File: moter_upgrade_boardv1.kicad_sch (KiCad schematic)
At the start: 52 parts, among them J1 Conn_01x04_Socket, J2 Conn_01x03_Socket, J3 Conn_01x02_Socket, J4 Conn_01x03_Socket, J5 Conn_01x05_Socket, J6 USB_C_Receptacle_USB2.0_16P, J7 Conn_01x03_Socket, SW1 SW_SPDT, SW2 SW_Push, SW3 SW_Wuerth_450301014042, U1 BD33FC0FP, U2 TLP785, U3 TLP785, U4 STM32H523CCTx, U5 MCP2562-E-P, U6 CH340E, U7 BD33FC0FP

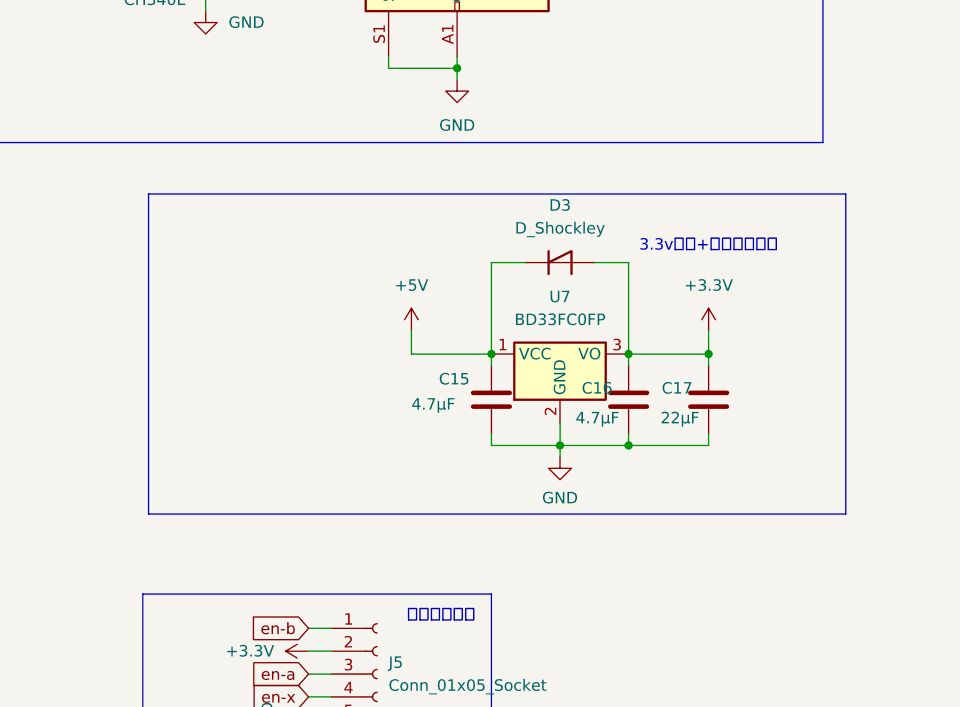
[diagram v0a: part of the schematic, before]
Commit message: 回路図の書き換え　部品配置配線のリセット
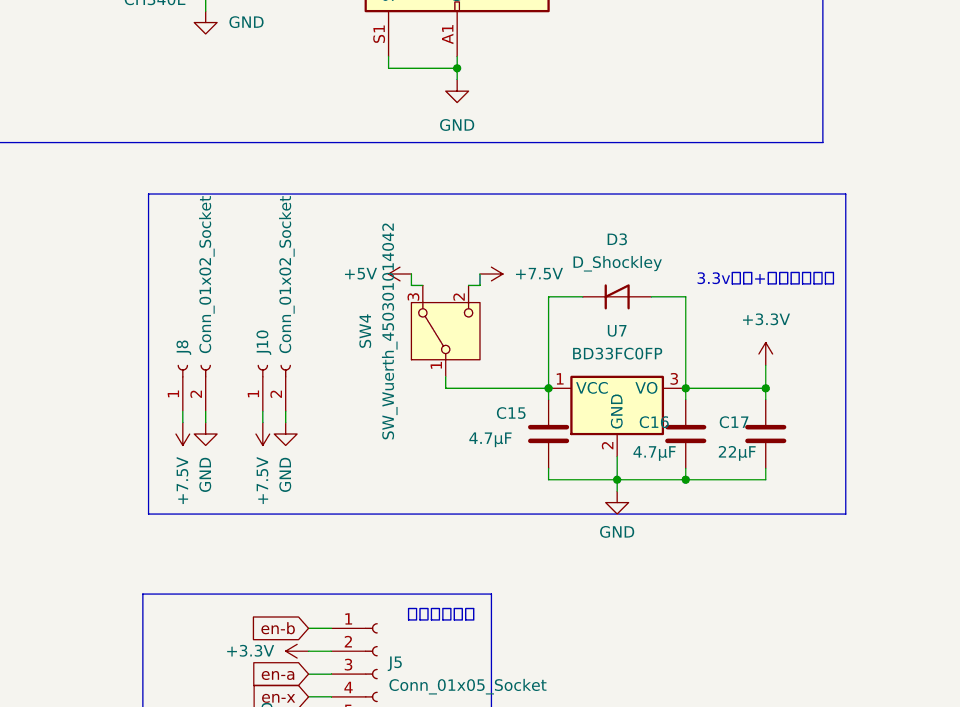
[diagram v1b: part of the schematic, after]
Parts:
- added J10, J8: Conn_01x02_Socket, symbol Connector:Conn_01x02_Socket
- added SW4: SW_Wuerth_450301014042, Button_Switch_THT:SW_Slide-03_Wuerth-WS-SLTV_10x2.5x6.4_P2.54mm, symbol Switch:SW_Wuerth_450301014042
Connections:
- net +5V: now also SW4.3 (A); no longer C15.1, D3.1 (K), U7.1 (VCC)
- net GND: now also J10.2 (Pin_2), J8.2 (Pin_2)
- new net: C15.1, D3.1 (K), SW4.1 (B), U7.1 (VCC)
- new net +7.5V: J10.1 (Pin_1), J8.1 (Pin_1), SW4.2 (C)
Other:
- moved on the sheet: C15, C16, C17, D3, U7

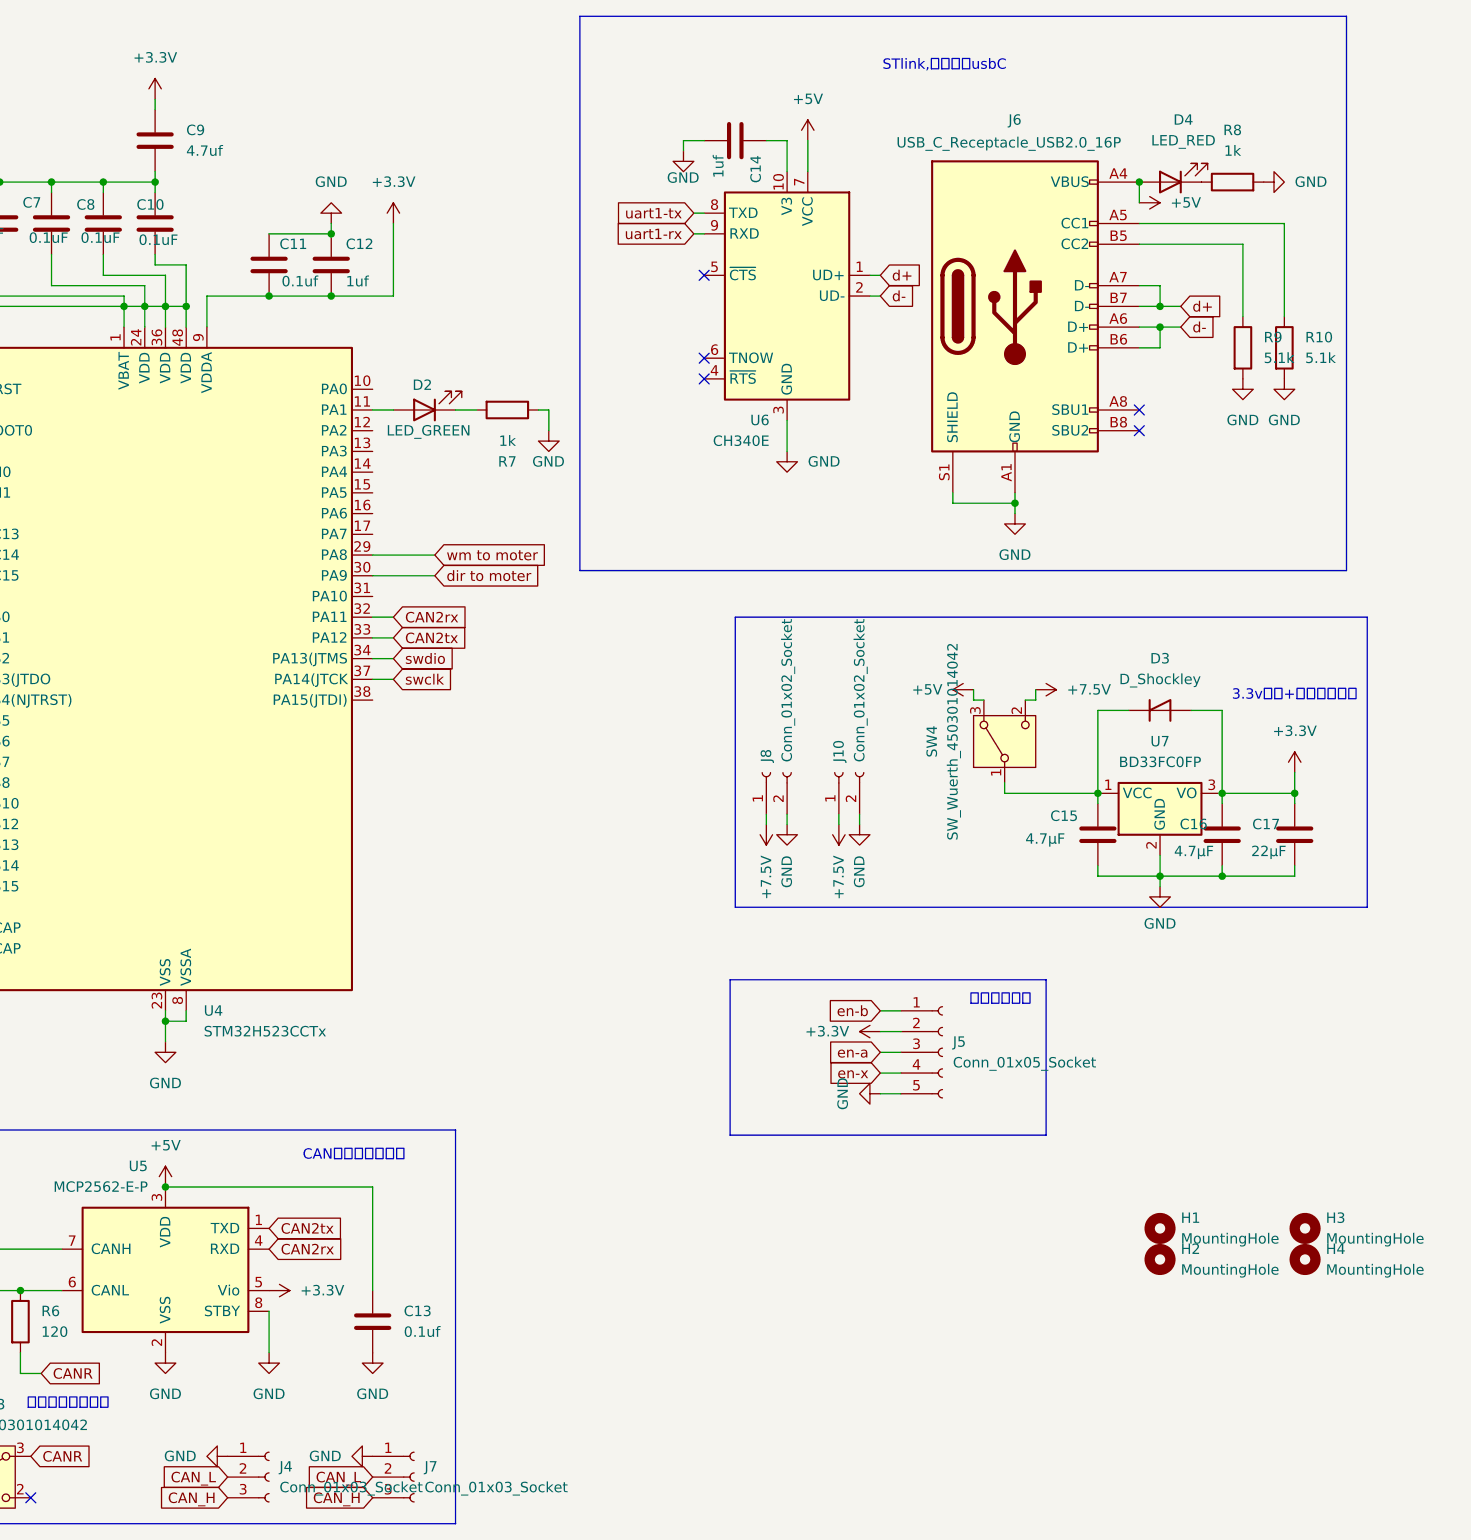
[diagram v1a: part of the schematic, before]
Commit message: 電源供給を切り替えられるように変更 部品配置の変更
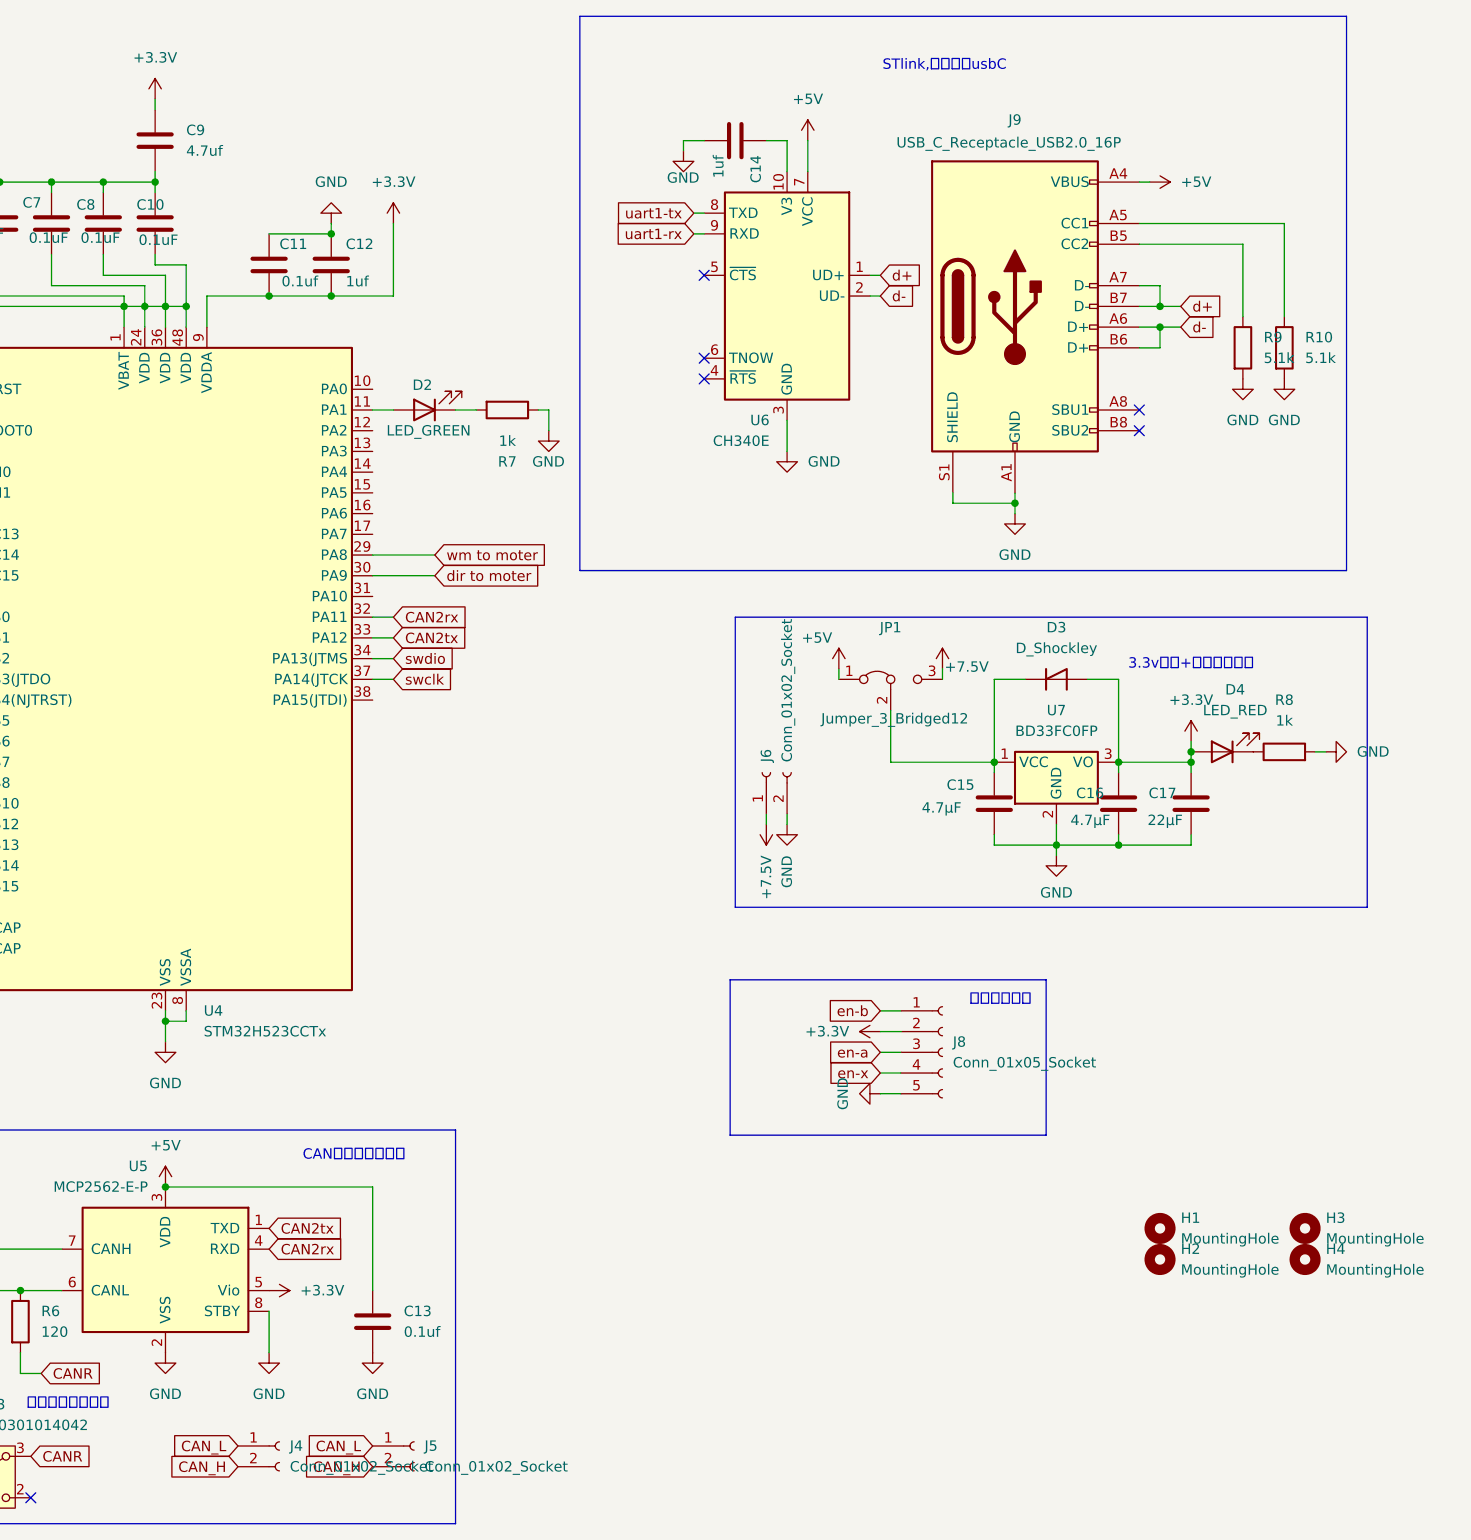
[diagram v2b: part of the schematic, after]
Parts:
- removed J10: Conn_01x02_Socket, symbol Connector:Conn_01x02_Socket
- removed J4: Conn_01x03_Socket, Connector_JST:JST_XH_S3B-XH-A-1_1x03_P2.50mm_Horizontal, symbol Connector:Conn_01x03_Socket
- removed J7: Conn_01x03_Socket, Connector_JST:JST_XH_B3B-XH-A_1x03_P2.50mm_Vertical, symbol Connector:Conn_01x03_Socket
- removed SW4: SW_Wuerth_450301014042, Button_Switch_THT:SW_Slide-03_Wuerth-WS-SLTV_10x2.5x6.4_P2.54mm, symbol Switch:SW_Wuerth_450301014042
- added J4, J5: Conn_01x02_Socket, Connector_JST:JST_XH_S2B-XH-A-1_1x02_P2.50mm_Horizontal, symbol Connector:Conn_01x02_Socket
- added JP1: Jumper_3_Bridged12, Connector_PinSocket_2.54mm:PinSocket_1x03_P2.54mm_Vertical, symbol Jumper:Jumper_3_Bridged12
- C5: footprint Capacitor_SMD:C_0805_2012Metric_Pad1.18x1.45mm_HandSolder -> Capacitor_SMD:C_0603_1608Metric_Pad1.08x0.95mm_HandSolder
- J6: renamed from J8; footprint (none) -> Connector_AMASS:AMASS_XT30PW-M_1x02_P2.50mm_Horizontal
- renumbered J5 to J8, J6 to J9
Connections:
- net +3.3V: now also D4.2 (A)
- net +5V: now also JP1.1 (A); no longer D4.2 (A)
- net +7.5V: now also JP1.3 (B)
- net CAN_H: now also J4.2 (Pin_2), J5.2 (Pin_2)
- net CAN_L: now also J4.1 (Pin_1), J5.1 (Pin_1)
- net at C15.1, D3.1 (K), U7.1 (VCC): now also JP1.2 (C)
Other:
- moved on the sheet: C15, C16, C17, D3, D4, R8, U7

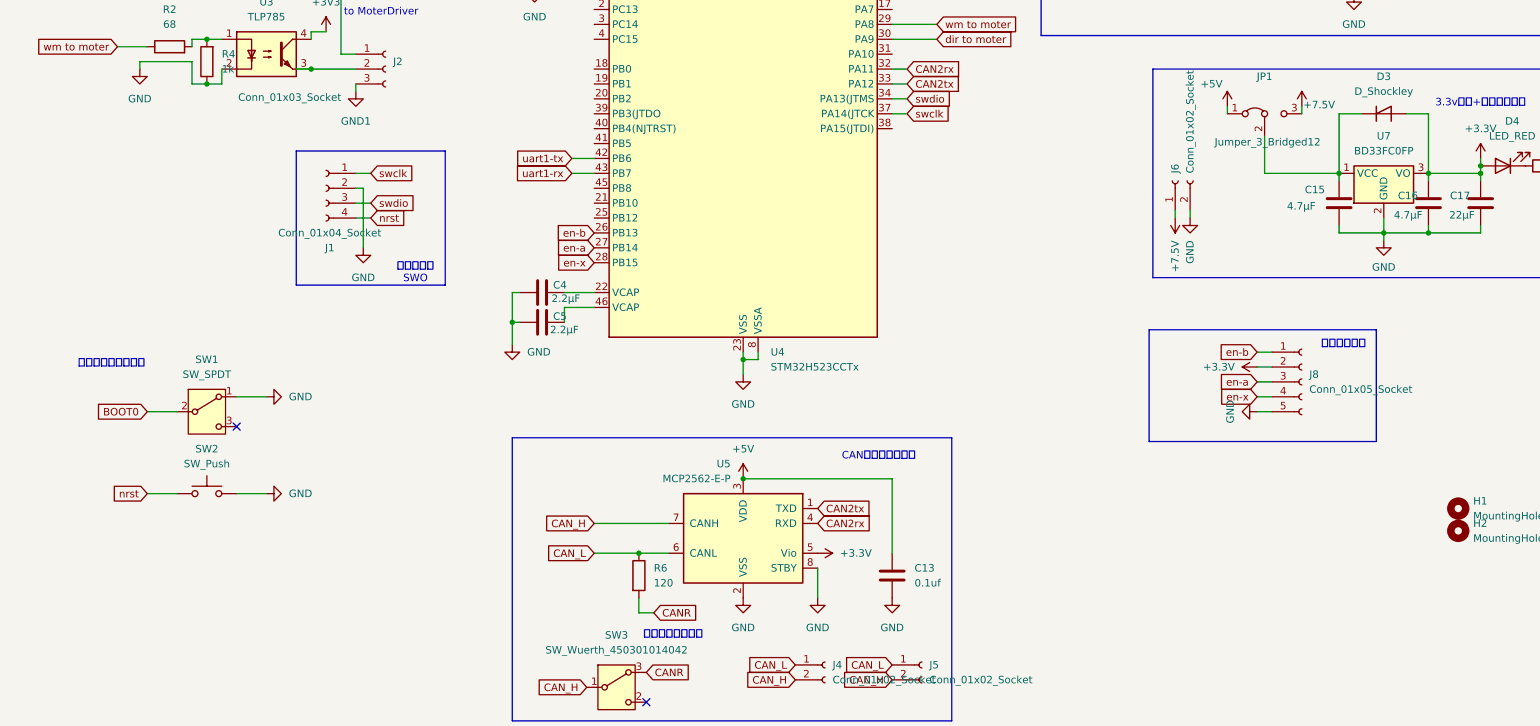
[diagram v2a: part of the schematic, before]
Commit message: stlinkをstdc14に対応させた　部品配置の変更
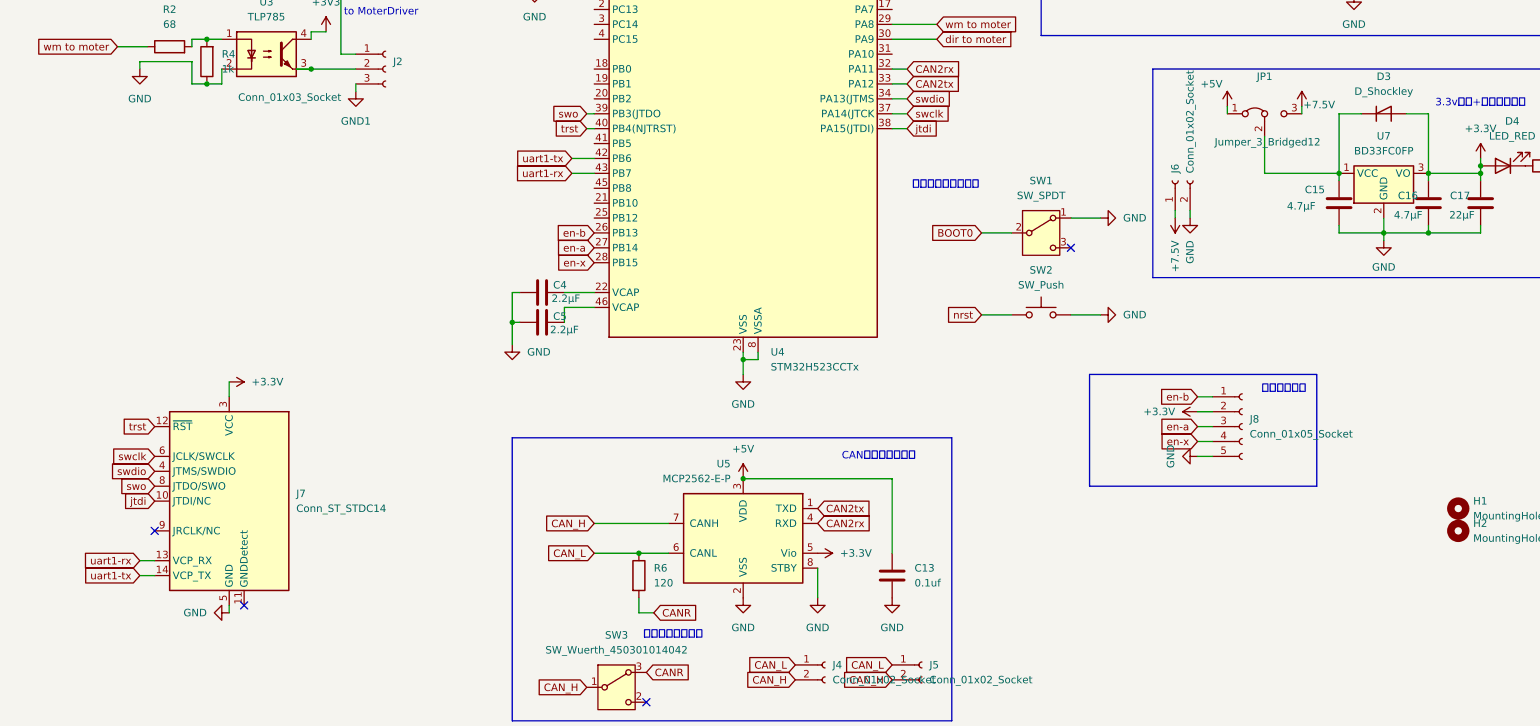
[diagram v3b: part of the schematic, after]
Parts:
- removed J1: Conn_01x04_Socket, Connector_PinHeader_2.54mm:PinHeader_1x04_P2.54mm_Vertical, symbol Connector:Conn_01x04_Socket
- added J7: Conn_ST_STDC14, Connector_PinHeader_1.27mm:PinHeader_2x07_P1.27mm_Vertical, symbol Connector:Conn_ST_STDC14
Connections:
- net +3.3V: now also J7.3 (VCC)
- net GND: now also J7.5 (GND), J7.7 (GND)
- net swclk: now also J7.6 (JCLK/SWCLK)
- net swdio: now also J7.4 (JTMS/SWDIO)
- net uart1-rx: now also J7.13 (VCP_RX)
- net uart1-tx: now also J7.14 (VCP_TX)
- net jtdi: now reaches U4.38 (PA15(JTDI))
- net jtdi: now also J7.10 (JTDI/NC)
- net swo: now reaches U4.39 (PB3(JTDO)
- net swo: now also J7.8 (JTDO/SWO)
- net trst: now reaches U4.40 (PB4(NJTRST))
- net trst: now also J7.12 (~{RST})
- no-connect marks 7 -> 9
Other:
- note removed: "デバッグ用 SWO"
- moved on the sheet: J8, SW1, SW2
